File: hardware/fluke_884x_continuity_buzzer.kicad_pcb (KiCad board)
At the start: 4 copper layers, 70.8 x 59.8 mm, 66 parts, among them J2 Conn_01x02, J203 16 pin DIP socket, J204 16 pin DIP socket, J3 USB_B_Micro, P203 16 pin DIP plug, P204 16 pin DIP plug, U1 AZ117EH-3.3, U2 W25Q128JVS, U3 RP2040, U4 umw_78l05_sot23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

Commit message: updating for rev3
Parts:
- removed C101: 10u, Capacitor_SMD:C_0805_2012Metric
- removed R22: 10k, Resistor_SMD:R_0402_1005Metric
- removed U4: umw_78l05_sot23, Package_TO_SOT_SMD:SOT-23-3
- removed U5: SN74LVC8T245PW, Package_SO:TSSOP-24_4.4x7.8mm_P0.65mm
- added C18: 220uF, Capacitor_THT:C_Radial_D6.3mm_H11.0mm_P2.50mm, F.Cu at (132.7, 33.1)
- J3: footprint Connector_USB:USB_Micro-B_Amphenol_10118194_Horizontal -> RP2040_minimal:USB_Micro-B_Amphenol_10118194_Horizontal
- TP1: footprint TestPoint:TestPoint_THTPad_D1.0mm_Drill0.5mm -> RP2040_minimal:TestPoint_Keystone_5019_Minature
- moved D1 7.53 mm to (125.8, 32.1)
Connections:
- U3 pad 11: RL0_3V -> /GPIO8
- U3 pad 2: RL3_3V -> /GPIO0
- U3 pad 3: RL5_3V -> /GPIO1
- U3 pad 4: RL2_3V -> /GPIO2
- U3 pad 5: RL4_3V -> /GPIO3
- U3 pad 6: RL6_3V -> /GPIO4
- U3 pad 8: RL1_3V -> /GPIO6
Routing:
- net /GPIO26_ADC0: track 51.1 -> 0.00 mm, vias 2 -> 0
- net +5V: track 38.1 -> 0.00 mm, vias 2 -> 0
- net /GPIO27_ADC1: track 32.1 -> 0.00 mm, vias 2 -> 0
- net RL6_3V: track 24.9 -> 0.00 mm, vias 2 -> 0
- net RL3_3V: track 24.6 -> 0.00 mm, vias 2 -> 0
- net RL2_3V: track 22.9 -> 0.00 mm, vias 2 -> 0
- net RL5_3V: track 22.3 -> 0.00 mm, vias 2 -> 0
- net RL0_3V: track 22.2 -> 0.00 mm, vias 2 -> 0
- net RL1_3V: track 22.0 -> 0.00 mm, vias 2 -> 0
- net RL4_3V: track 21.2 -> 0.00 mm, vias 2 -> 0
- net Net-(D1-K): track 45.5 -> 58.7 mm
- net /RL0: track 25.0 -> 14.9 mm, vias 1 -> 0
- net /RL1: track 23.1 -> 14.9 mm, vias 1 -> 0
- net /F2: track 31.9 -> 23.9 mm
- net GND: track 64.5 -> 57.3 mm, vias 37 -> 36
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- removed copper zone on F.Cu, net Net-(D1-K)
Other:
- board text added: "(C) Ned Konz 2024 Rev. ${REVISION}"
- board text removed: "(C) Ned Konz, 2/2024 Rev. 2"

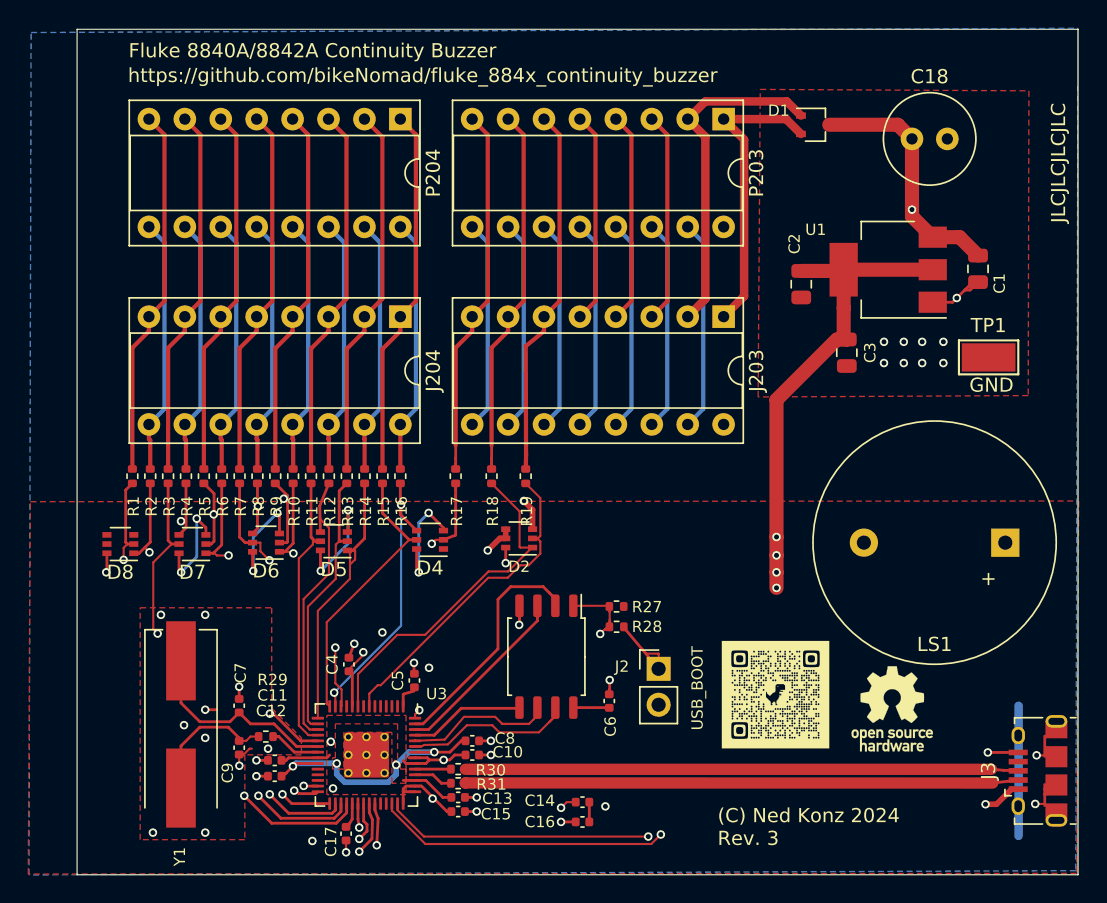
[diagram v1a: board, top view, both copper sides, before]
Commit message: Add final parts; generate JLCPCB data
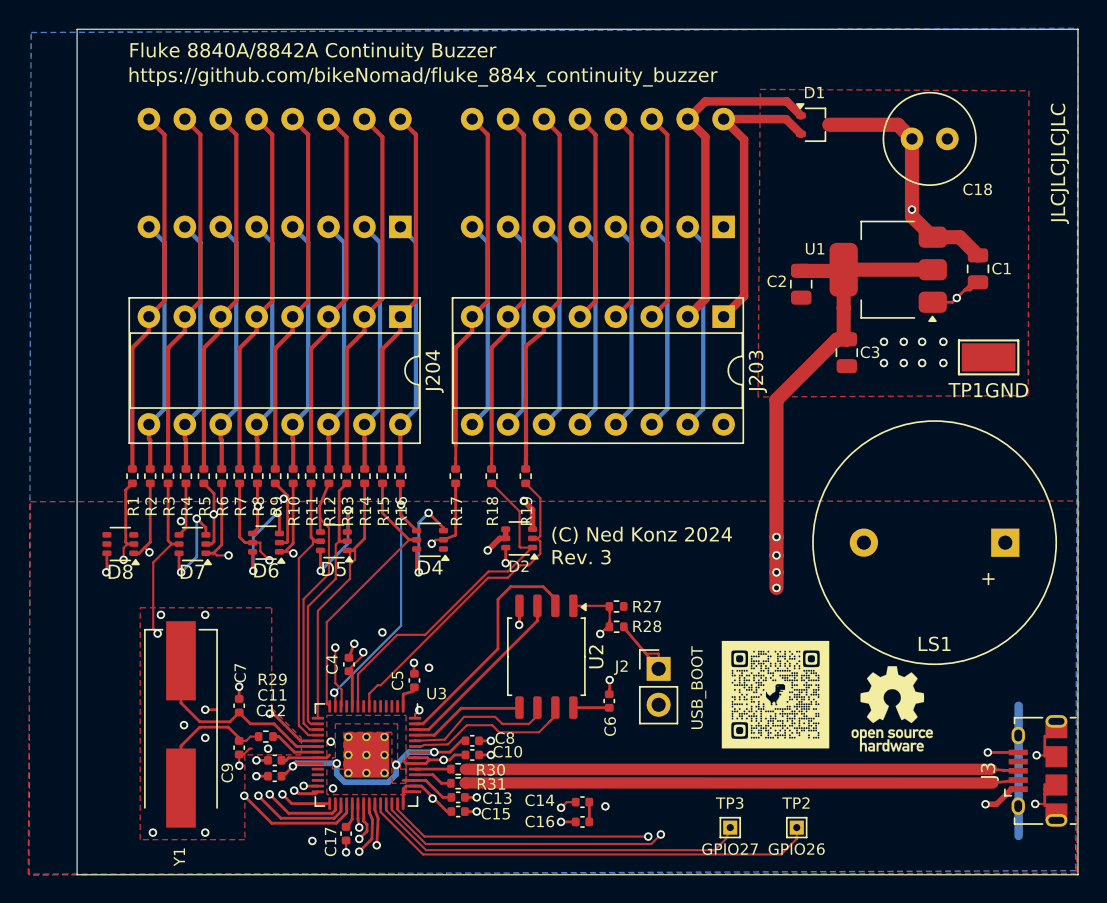
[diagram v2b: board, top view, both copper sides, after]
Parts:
- added TP2: GPIO26, TestPoint:TestPoint_THTPad_1.0x1.0mm_Drill0.5mm, F.Cu at (124.5, 81.8)
- added TP3: GPIO27, TestPoint:TestPoint_THTPad_1.0x1.0mm_Drill0.5mm, F.Cu at (119.8, 81.8)
- LS1: value Speaker_Crystal -> Piezo Transducer
- P203, P204: footprint Package_DIP:DIP-16_W7.62mm_Socket -> RP2040_minimal:DIP-16_W7.62mm; moved to B.Cu
- U2: footprint Package_SO:SOIC-8_5.23x5.23mm_P1.27mm -> RP2040_minimal:SOIC-8_5.23x5.23mm_P1.27mm
- moved P203 7.62 mm to (119.4, 39.4), turned to 90 degrees
- moved P204 7.62 mm to (96.5, 39.4), turned to 90 degrees
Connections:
- P203 pad 1: /F1 -> GND
- P203 pad 10: /RL1 -> /G7
- P203 pad 11: /RL6 -> /G5
- P203 pad 12: /RL4 -> /S0
- P203 pad 13: /RL2 -> /S1
- P203 pad 14: /RL5 -> /S2
- P203 pad 15: /RL3 -> /F2
- P203 pad 16: GND -> /F1
- P203 pad 2: /F2 -> /RL3
- P203 pad 3: /S2 -> /RL5
- P203 pad 4: /S1 -> /RL2
- P203 pad 5: /S0 -> /RL4
- P203 pad 6: /G5 -> /RL6
- P203 pad 7: /G7 -> /RL1
- P203 pad 8: /G6 -> /RL0
- P203 pad 9: /RL0 -> /G6
- P204 pad 1: /PDP -> /G2
- P204 pad 10: /Pa -> /PS3
- P204 pad 11: /Pc -> /Pg
- P204 pad 12: /G0 -> /Pf
- P204 pad 13: /G1 -> /Pe
- P204 pad 14: /G4 -> /Pd
- P204 pad 15: /G3 -> /PS1
- P204 pad 16: /G2 -> /PDP
- P204 pad 2: /PS1 -> /G3
- P204 pad 3: /Pd -> /G4
- P204 pad 4: /Pe -> /G1
- P204 pad 5: /Pf -> /G0
- P204 pad 6: /Pg -> /Pc
- P204 pad 7: /PS3 -> /Pa
- P204 pad 8: /PS2 -> /Pb
- P204 pad 9: /Pb -> /PS2
- U3 pad 24: /SWCLK -> unconnected-(U3-SWCLK-Pad24)
- U3 pad 25: /SWD -> unconnected-(U3-SWD-Pad25)
- U3 pad 26: /RUN -> unconnected-(U3-RUN-Pad26)
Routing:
- net /GPIO26_ADC0: track 0.00 -> 32.5 mm
- net /GPIO27_ADC1: track 0.00 -> 26.9 mm
- added copper zone on In1.Cu, net GND
- added copper zone on In2.Cu, net GND
